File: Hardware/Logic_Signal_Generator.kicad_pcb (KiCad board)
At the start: 2 copper layers, 51 parts, among them J1 JTAG, J2 I/O, J3 USB_B, J4 POWER_OUT, Q1 DMG3414U, Q2 DMG3414U, Q3 DMG3414U, Q4 DMG3414U, Q5 DMG3414U, Q6 DMG3414U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

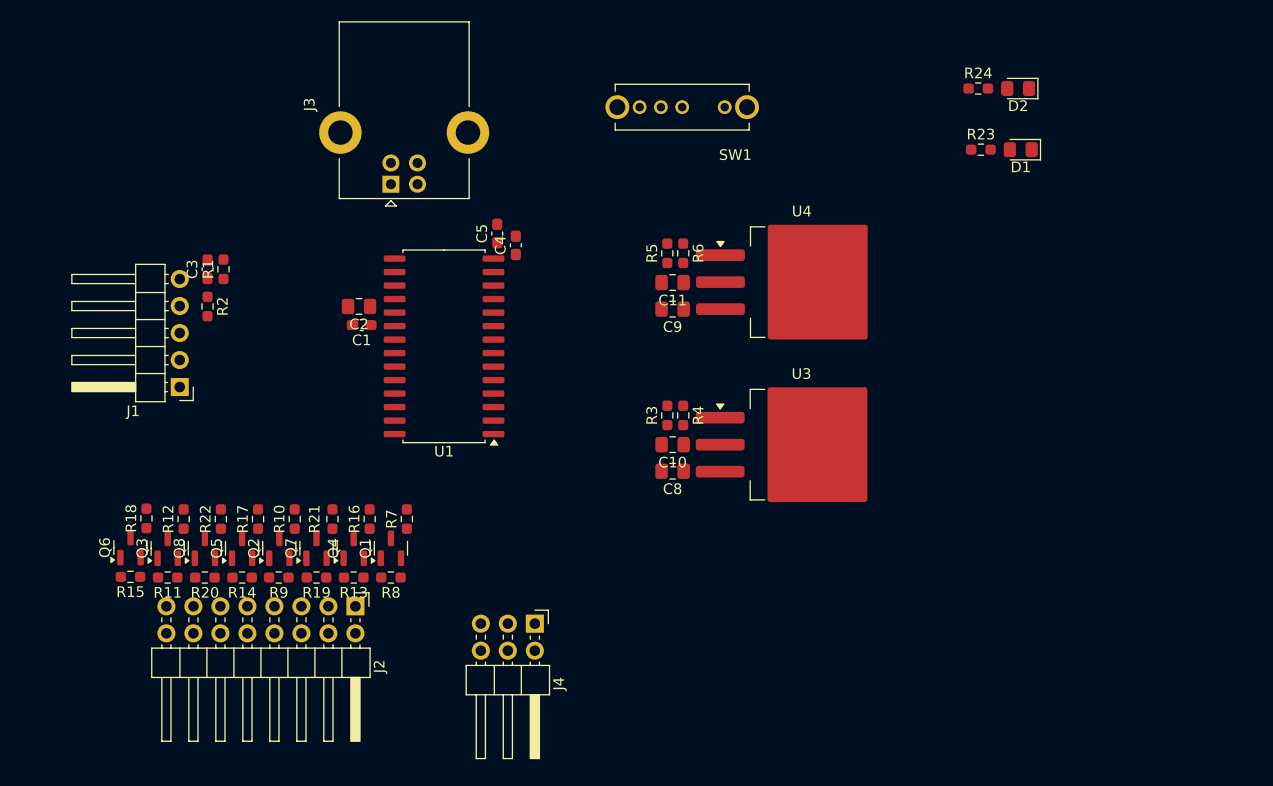
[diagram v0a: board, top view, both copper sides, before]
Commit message: [Hardware] Added the mounting holes and the PCB edges.
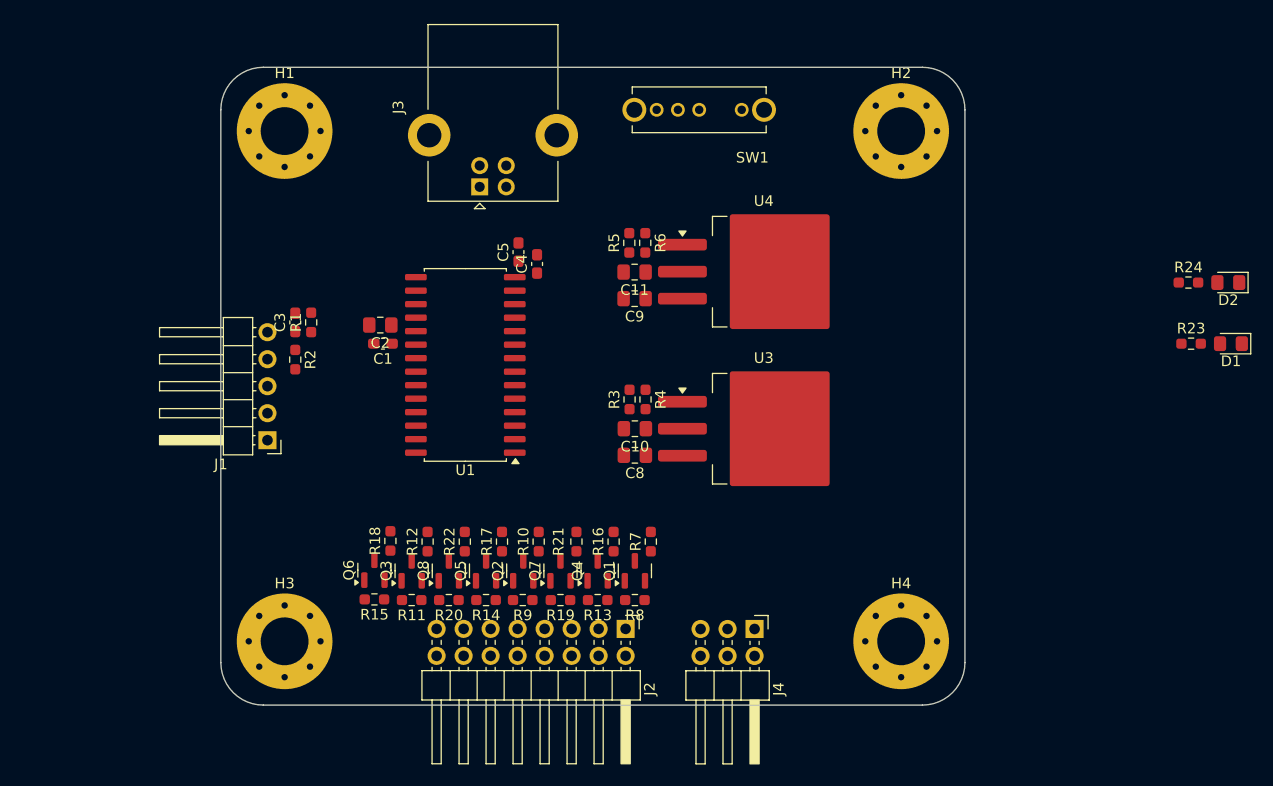
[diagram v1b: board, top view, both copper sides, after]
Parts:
- added H1: Hole, MountingHole:MountingHole_4.5mm_Pad_Via, F.Cu at (134.0, 85.0)
- added H2: Hole, MountingHole:MountingHole_4.5mm_Pad_Via, F.Cu at (192.0, 85.0)
- added H3: Hole, MountingHole:MountingHole_4.5mm_Pad_Via, F.Cu at (134.0, 133.0)
- added H4: Hole, MountingHole:MountingHole_4.5mm_Pad_Via, F.Cu at (192.0, 133.0)
- moved D1 26.9 mm to (223.0, 105.0)
- moved D2 26.9 mm to (222.8, 99.2)
- moved R23 26.9 mm to (219.3, 105.0)
- moved R24 26.9 mm to (219.0, 99.2)
- moved J2 25.5 mm to (166.1, 131.8)
- moved R10 23.0 mm to (157.9, 123.6)
- moved R9 23.0 mm to (156.4, 129.1)
- moved Q1 23.0 mm to (166.9, 126.4)
- moved Q2 23.0 mm to (156.4, 126.4)
- moved Q3 23.0 mm to (145.9, 126.4)
- moved Q4 23.0 mm to (163.4, 126.4)
- moved Q5 23.0 mm to (152.9, 126.4)
- moved Q6 23.0 mm to (142.4, 126.3)
- moved Q7 23.0 mm to (159.9, 126.4)
- moved Q8 23.0 mm to (149.4, 126.4)
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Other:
- board outline added: 70 x 60 mm

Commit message: [Hardware] Enabled PCB teardrops.
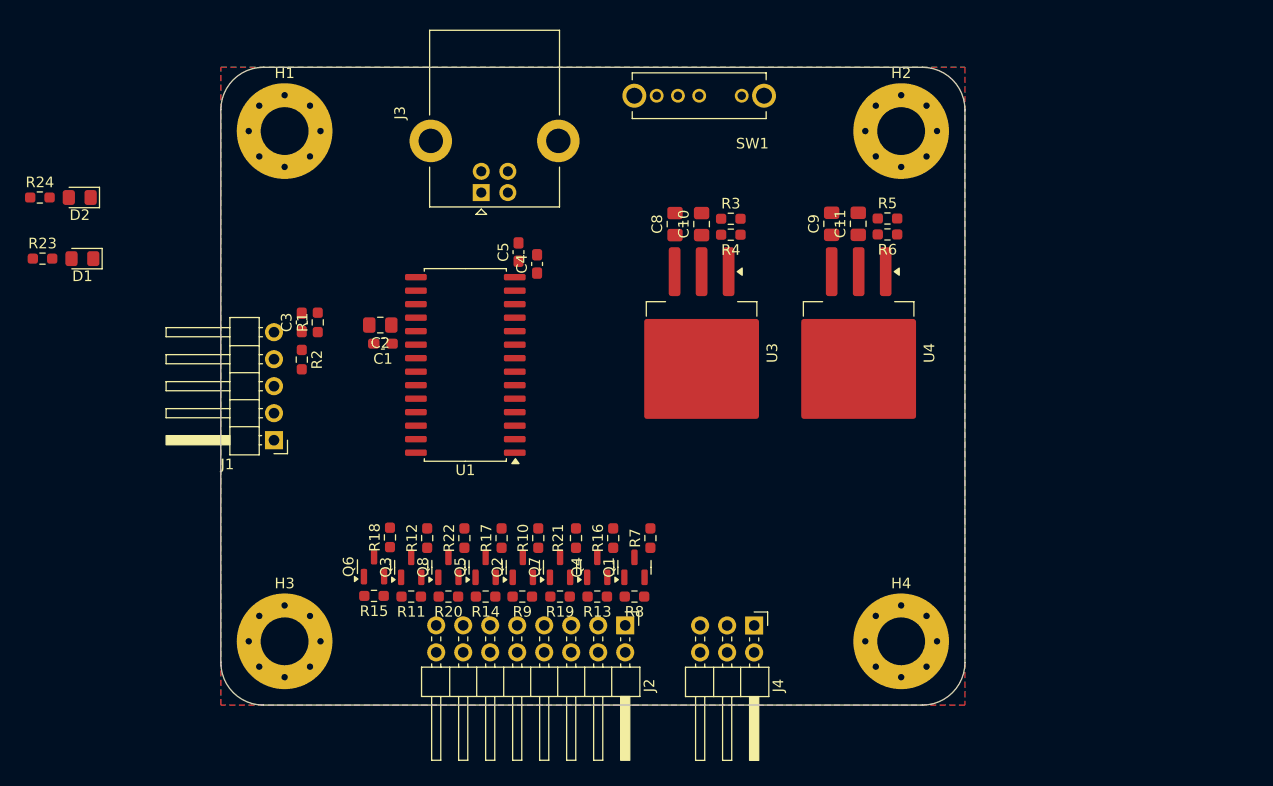
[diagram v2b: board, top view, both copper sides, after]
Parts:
- moved D1 108.3 mm to (115.0, 97.0)
- moved D2 108.3 mm to (114.7, 91.2)
- moved R23 108.3 mm to (111.2, 97.0)
- moved R24 108.3 mm to (111.0, 91.2)
- moved R5 24.4 mm to (190.7, 93.2), turned to 0 degrees
- moved R6 22.8 mm to (190.7, 94.7), turned to 180 degrees
- moved C8 22.1 mm to (170.7, 93.8), turned to 90 degrees
- moved C11 21.5 mm to (188.0, 93.7), turned to 90 degrees
- moved C10 20.2 mm to (173.2, 93.8), turned to 90 degrees
- moved C9 19.8 mm to (185.5, 93.7), turned to 90 degrees
- moved R3 19.5 mm to (176.0, 93.2), turned to 0 degrees
- moved R4 17.5 mm to (176.0, 94.8), turned to 180 degrees
- moved U4 11.8 mm to (188.0, 105.9), turned to -90 degrees
- moved U3 9.22 mm to (173.2, 105.9), turned to -90 degrees
- moved SW1 1.33 mm to (173.0, 81.7)
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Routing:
- added copper zone on B.Cu, net GND
- added copper zone on F.Cu, net GND
